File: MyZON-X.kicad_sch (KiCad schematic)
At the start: 29 parts, among them J1 Connector ZX81, SW1 SW_DIP_x03, U1 AY-3-8910, U2. 74HCT74, U3. 74HCT08, U4 74HCT11, U4. 74HCT11, U5. 74HCT02

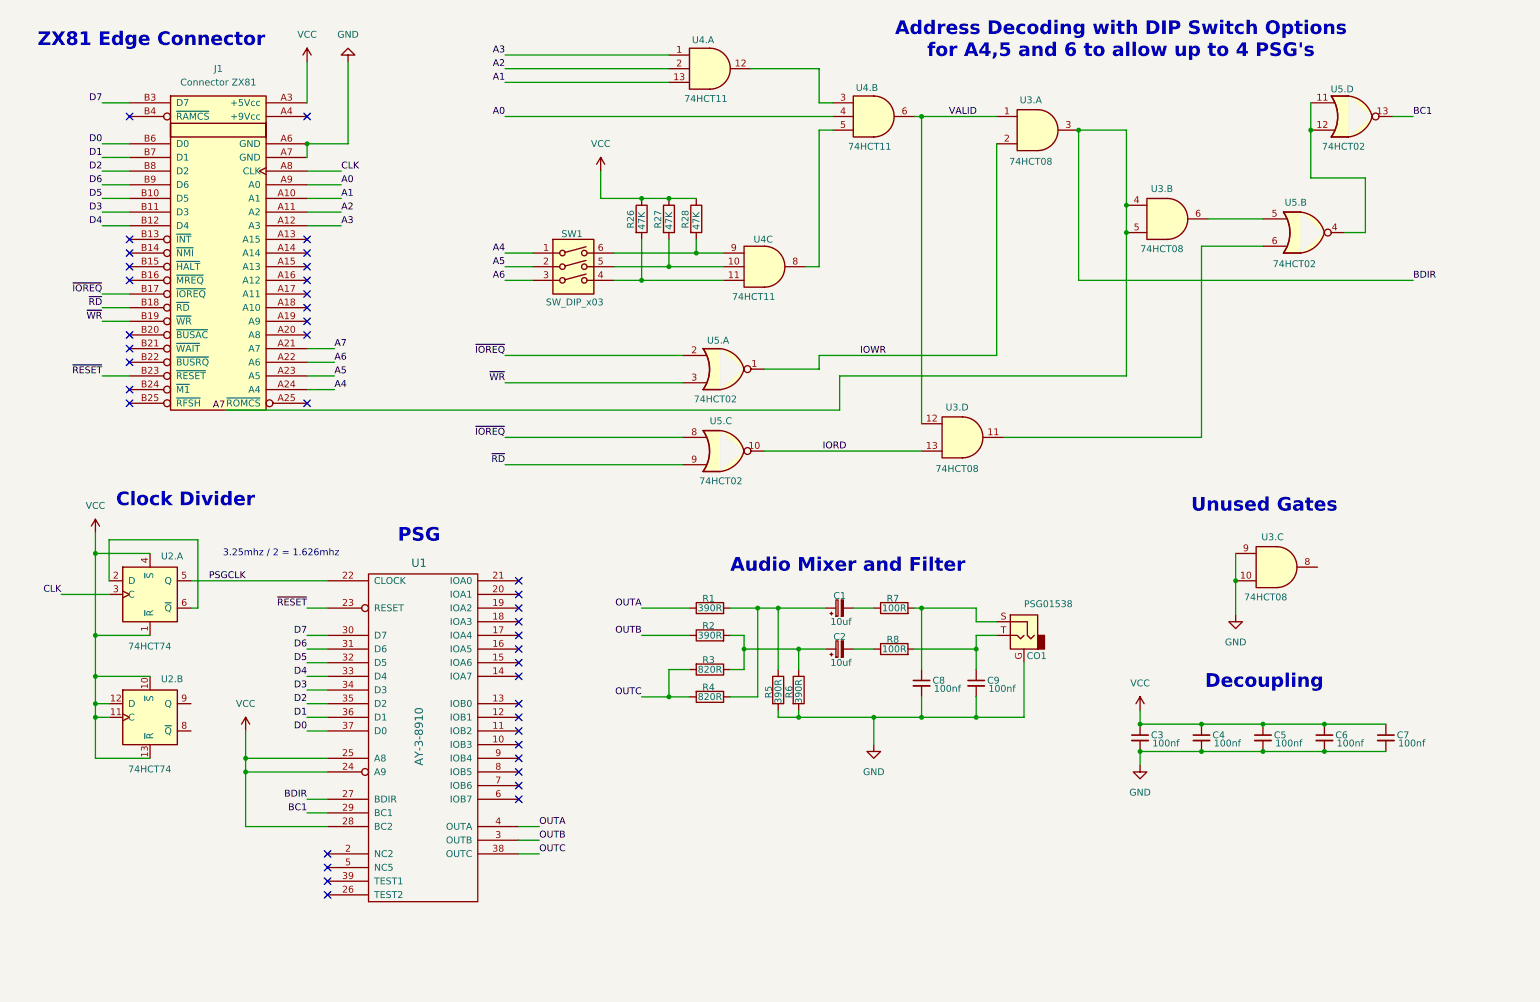
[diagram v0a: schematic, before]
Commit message: A7 was missaligned Added text to show detail of channel mixing on audio
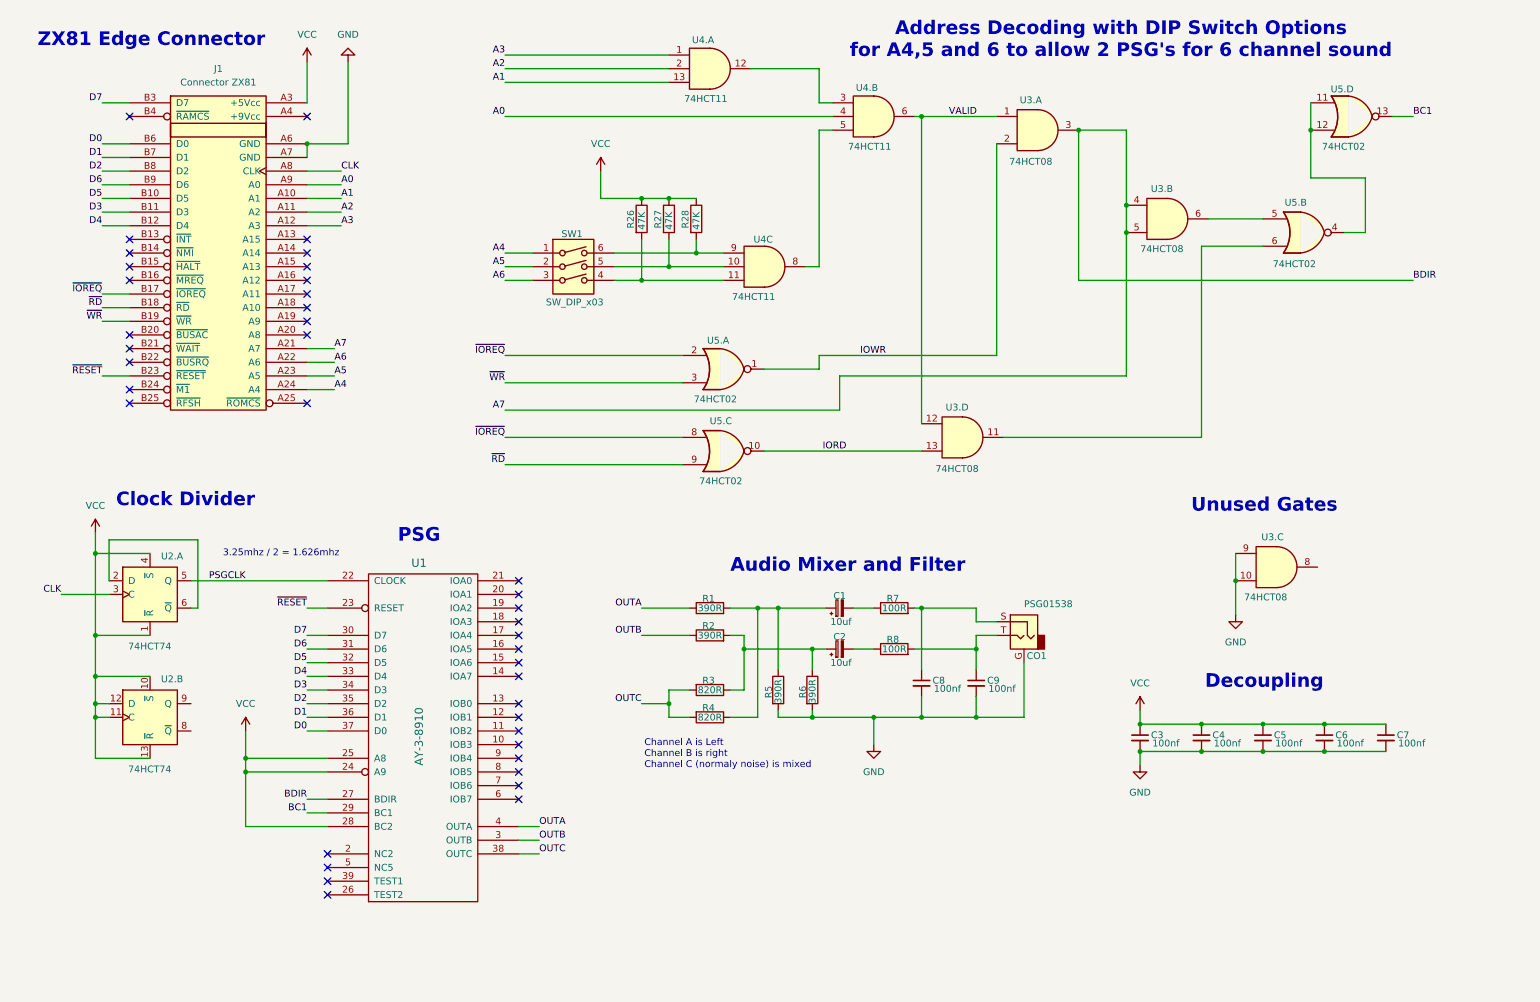
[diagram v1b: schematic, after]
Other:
- note added: "Address Decoding with DIP Switch Options for A4,5 and 6 to allow 2 PSG's for 6 channel sound"
- note added: "Channel A is Left Channel B is right Channel C (normaly noise) is mixed"
- note removed: "Address Decoding with DIP Switch Options for A4,5 and 6 to allow up to 4 PSG's"
- moved on the sheet: R3, R4, R6
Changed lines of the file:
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@@
 		(rev "1.0")
 	)
-	(text "Address Decoding with DIP Switch Options \nfor A4,5 and 6 to allow up to 4 PSG's"
+	(text "Address Decoding with DIP Switch Options \nfor A4,5 and 6 to allow 2 PSG's for 6 channel sound"
 		(exclude_from_sim no)
 		(at 219.964 20.066 0)
@@
 		)
 	)
+	(text "Channel A is Left\nChannel B is right\nChannel C (normaly noise) is mixed"
+		(exclude_from_sim no)
+		(at 131.318 152.908 0)
+		(effects
+			(font
+				(size 1.27 1.27)
+			)
+			(justify left)
+		)
+	)
 	(text "Audio Mixer and Filter"
 		(exclude_from_sim no)
@@
 	)
 	(junction
-		(at 135.89 142.24)
-		(diameter 0)
-		(color 0 0 0 0)
-	)
-	(junction
-		(at 160.02 133.35)
-		(diameter 0)
-		(color 0 0 0 0)
-	)
-	(junction
 		(at 135.89 49.53)
 		(diameter 0)
@@
 	)
 	(junction
-		(at 220.98 55.88)
+		(at 162.56 146.05)
 		(diameter 0)
 		(color 0 0 0 0)
 	)
 	(junction
-		(at 193.04 133.35)
+		(at 220.98 55.88)
 		(diameter 0)
 		(color 0 0 0 0)
 	)
 	(junction
-		(at 246.38 152.4)
+		(at 193.04 133.35)
 		(diameter 0)
 		(color 0 0 0 0)
 	)
 	(junction
-		(at 160.02 146.05)
+		(at 246.38 152.4)
 		(diameter 0)
 		(color 0 0 0 0)
@@
 	)
 	(junction
+		(at 135.89 143.51)
+		(diameter 0)
+		(color 0 0 0 0)
+	)
+	(junction
+		(at 162.56 133.35)
+		(diameter 0)
+		(color 0 0 0 0)
+	)
+	(junction
 		(at 182.88 34.29)
 		(diameter 0)
@@
 	(wire
 		(pts
-			(xy 149.86 137.16) (xy 149.86 133.35)
+			(xy 149.86 140.97) (xy 149.86 133.35)
 		)
 		(stroke
@@
 	(wire
 		(pts
-			(xy 160.02 133.35) (xy 165.1 133.35)
-		)
-		(stroke
-			(width 0)
-			(type default)
-		)
-	)
-	(wire
-		(pts
-			(xy 147.32 137.16) (xy 149.86 137.16)
+			(xy 147.32 140.97) (xy 149.86 140.97)
 		)
 		(stroke
@@
 	(wire
 		(pts
-			(xy 135.89 137.16) (xy 135.89 142.24)
+			(xy 162.56 133.35) (xy 165.1 133.35)
 		)
 		(stroke
@@
 	(wire
 		(pts
-			(xy 160.02 137.16) (xy 160.02 133.35)
-		)
-		(stroke
-			(width 0)
-			(type default)
-		)
-	)
-	(wire
-		(pts
-			(xy 160.02 146.05) (xy 173.99 146.05)
+			(xy 162.56 137.16) (xy 162.56 133.35)
 		)
 		(stroke
@@
 	(wire
 		(pts
-			(xy 149.86 133.35) (xy 160.02 133.35)
+			(xy 149.86 133.35) (xy 162.56 133.35)
 		)
 		(stroke
@@
 	(wire
 		(pts
-			(xy 156.21 146.05) (xy 160.02 146.05)
+			(xy 156.21 146.05) (xy 162.56 146.05)
 		)
 		(stroke
@@
 	(wire
 		(pts
+			(xy 162.56 146.05) (xy 173.99 146.05)
+		)
+		(stroke
+			(width 0)
+			(type default)
+		)
+	)
+	(wire
+		(pts
 			(xy 193.04 146.05) (xy 201.93 146.05)
 		)
@@
 	(wire
 		(pts
-			(xy 130.81 142.24) (xy 135.89 142.24)
+			(xy 130.81 143.51) (xy 135.89 143.51)
 		)
 		(stroke
@@
 	(wire
 		(pts
-			(xy 167.64 88.9) (xy 53.34 88.9)
+			(xy 167.64 88.9) (xy 105.41 88.9)
 		)
 		(stroke
@@
 	(wire
 		(pts
-			(xy 147.32 142.24) (xy 152.4 142.24)
+			(xy 147.32 146.05) (xy 152.4 146.05)
 		)
 		(stroke
@@
 	(wire
 		(pts
+			(xy 135.89 140.97) (xy 135.89 143.51)
+		)
+		(stroke
+			(width 0)
+			(type default)
+		)
+	)
+	(wire
+		(pts
 			(xy 31.75 113.03) (xy 48.26 113.03)
 		)
@@
 	(wire
 		(pts
-			(xy 160.02 144.78) (xy 160.02 146.05)
+			(xy 162.56 144.78) (xy 162.56 146.05)
 		)
 		(stroke
@@
 	(wire
 		(pts
-			(xy 152.4 142.24) (xy 152.4 125.73)
+			(xy 152.4 146.05) (xy 152.4 125.73)
 		)
 		(stroke
@@
 	(wire
 		(pts
-			(xy 135.89 142.24) (xy 139.7 142.24)
+			(xy 135.89 146.05) (xy 139.7 146.05)
 		)
 		(stroke
@@
 	(wire
 		(pts
+			(xy 135.89 146.05) (xy 135.89 143.51)
+		)
+		(stroke
+			(width 0)
+			(type default)
+		)
+	)
+	(wire
+		(pts
 			(xy 111.76 168.91) (xy 107.95 168.91)
 		)
@@
 	(wire
 		(pts
-			(xy 139.7 137.16) (xy 135.89 137.16)
+			(xy 139.7 140.97) (xy 135.89 140.97)
 		)
 		(stroke
@@
 	)
 	(label "A7"
-		(at 53.34 88.9 180)
+		(at 105.41 88.9 180)
 		(effects
 			(font
@@
 	)
 	(label "OUTC"
-		(at 130.81 142.24 180)
+		(at 130.81 143.51 180)
 		(effects
 			(font
@@
 		(lib_name "R_4")
 		(lib_id "Device:R")
-		(at 143.51 137.16 270)
+		(at 143.51 140.97 270)
 		(unit 1)
 		(exclude_from_sim no)
@@
 		(dnp no)
 		(property "Reference" "R3"
-			(at 143.256 135.382 90)
+			(at 143.256 139.192 90)
 			(effects
 				(font
@@
 		)
 		(property "Value" "820R"
-			(at 143.51 137.16 90)
+			(at 143.51 140.97 90)
 			(effects
 				(font
@@
 		)
 		(property "Footprint" ""
-			(at 143.51 135.382 90)
+			(at 143.51 139.192 90)
 			(effects
 				(font
@@
 		)
 		(property "Datasheet" "~"
-			(at 143.51 137.16 0)
+			(at 143.51 140.97 0)
 			(effects
 				(font
@@
 		)
 		(property "Description" "Resistor"
-			(at 143.51 137.16 0)
+			(at 143.51 140.97 0)
 			(effects
 				(font
@@
 		(lib_name "R_8")
 		(lib_id "Device:R")
-		(at 160.02 140.97 0)
+		(at 162.56 140.97 0)
 		(unit 1)
 		(exclude_from_sim no)
@@
 		(dnp no)
 		(property "Reference" "R6"
-			(at 158.242 142.494 90)
+			(at 160.782 142.494 90)
 			(effects
 				(font
@@
 		)
 		(property "Value" "390R"
-			(at 160.02 143.51 90)
+			(at 162.56 143.51 90)
 			(effects
 				(font
@@
 		)
 		(property "Footprint" ""
-			(at 158.242 140.97 90)
+			(at 160.782 140.97 90)
 			(effects
 				(font
@@
 		)
 		(property "Datasheet" "~"
-			(at 160.02 140.97 0)
+			(at 162.56 140.97 0)
 			(effects
 				(font
@@
 		)
 		(property "Description" "Resistor"
-			(at 160.02 140.97 0)
+			(at 162.56 140.97 0)
 			(effects
 				(font
@@
 		(lib_name "R_3")
 		(lib_id "Device:R")
-		(at 143.51 142.24 270)
+		(at 143.51 146.05 270)
 		(unit 1)
 		(exclude_from_sim no)
@@
 		(dnp no)
 		(property "Reference" "R4"
-			(at 143.256 140.462 90)
+			(at 143.256 144.272 90)
 			(effects
 				(font
@@
 		)
 		(property "Value" "820R"
-			(at 143.51 142.24 90)
+			(at 143.51 146.05 90)
 			(effects
 				(font
@@
 		)
 		(property "Footprint" ""
-			(at 143.51 140.462 90)
+			(at 143.51 144.272 90)
 			(effects
 				(font
@@
 		)
 		(property "Datasheet" "~"
-			(at 143.51 142.24 0)
+			(at 143.51 146.05 0)
 			(effects
 				(font
@@
 		)
 		(property "Description" "Resistor"
-			(at 143.51 142.24 0)
+			(at 143.51 146.05 0)
 			(effects
 				(font

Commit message: Added Audio interconnect Added extra nots for Addressing
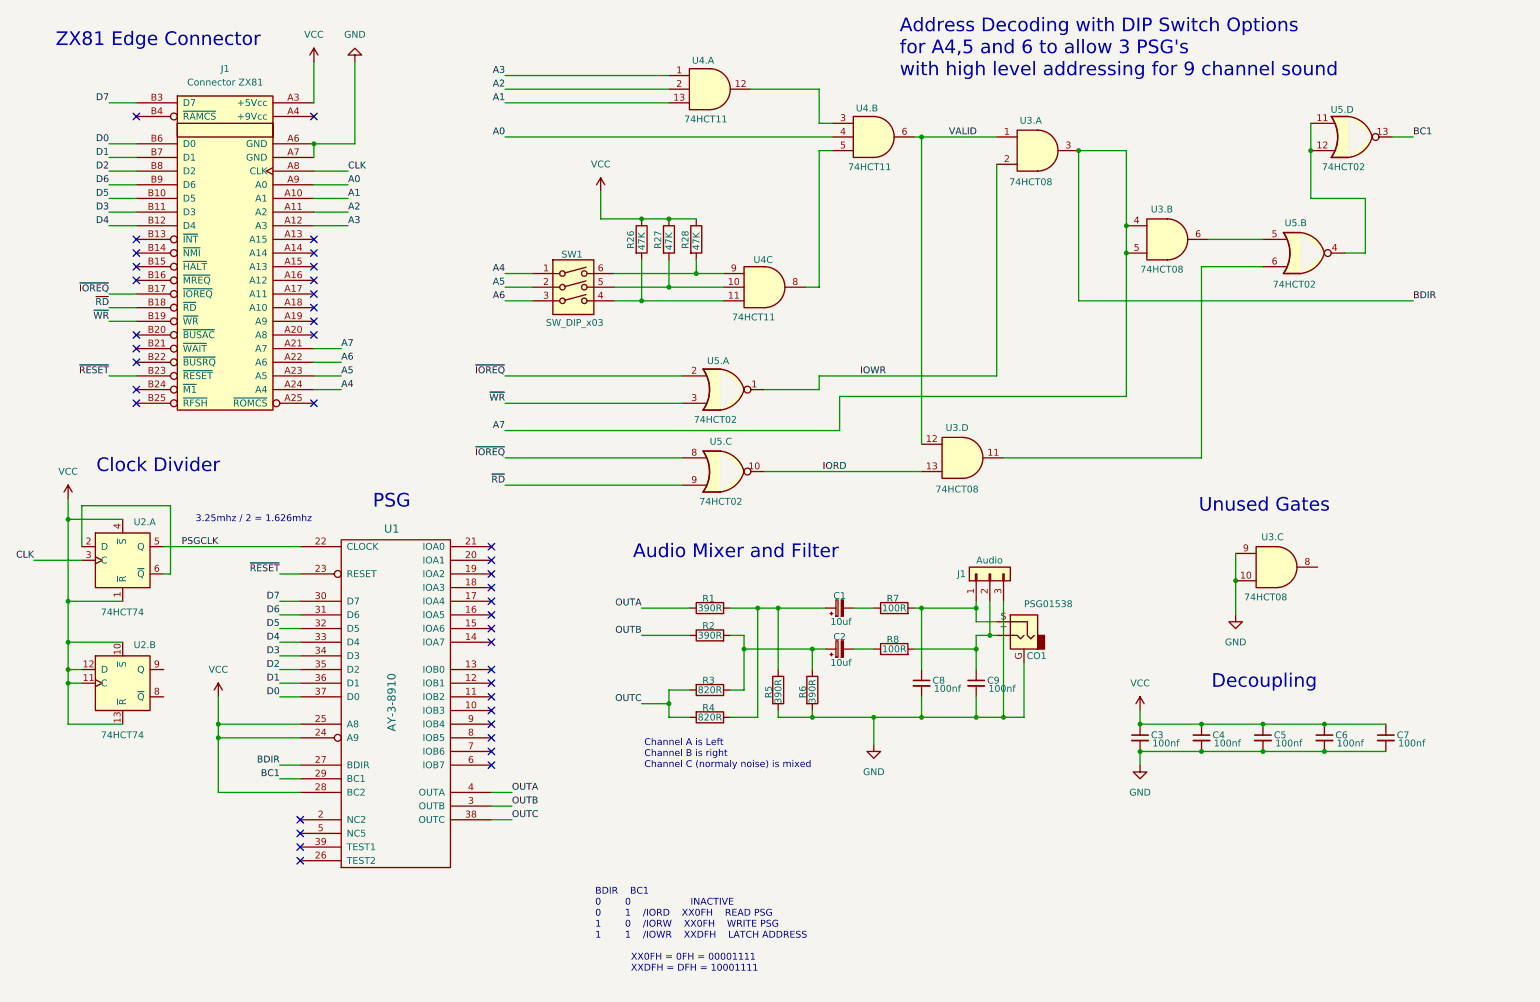
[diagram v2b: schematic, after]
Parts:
- added J1: Audio, symbol Connector_Generic:Conn_01x03
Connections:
- net GND: now also J1.3 (Pin_3)
- net at C9.1, CO1.T, R8.2: now also J1.2 (Pin_2)
- net at C8.1, CO1.S, R7.2: now also J1.1 (Pin_1)
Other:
- note added: "Address Decoding with DIP Switch Options for A4,5 and 6 to allow 3 PSG's with high level addressing for 9 channel sound"
- note added: "BDIR BC1 0 0 INACTIVE 0 1 /IORD XX0FH READ PSG 1 0 /IORW XX0FH WRITE PSG 1 1 /IOWR XXDFH LATCH ADDRESS XX0FH = 0FH = 00001111 XXDFH = DFH = 10001111"
- note removed: "Address Decoding with DIP Switch Options for A4,5 and 6 to allow 2 PSG's for 6 channel sound"
- moved on the sheet: J1, R26, R27, R28, SW1, U1, U2.A, U2.B, U3.A, U3.B, U3.D, U4.A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

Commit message: Added VCC and GND Added Power Suuply to IC's Commented 3 ERC warnings re bidirectional pins for 5v and GND for the ZX81 Connector
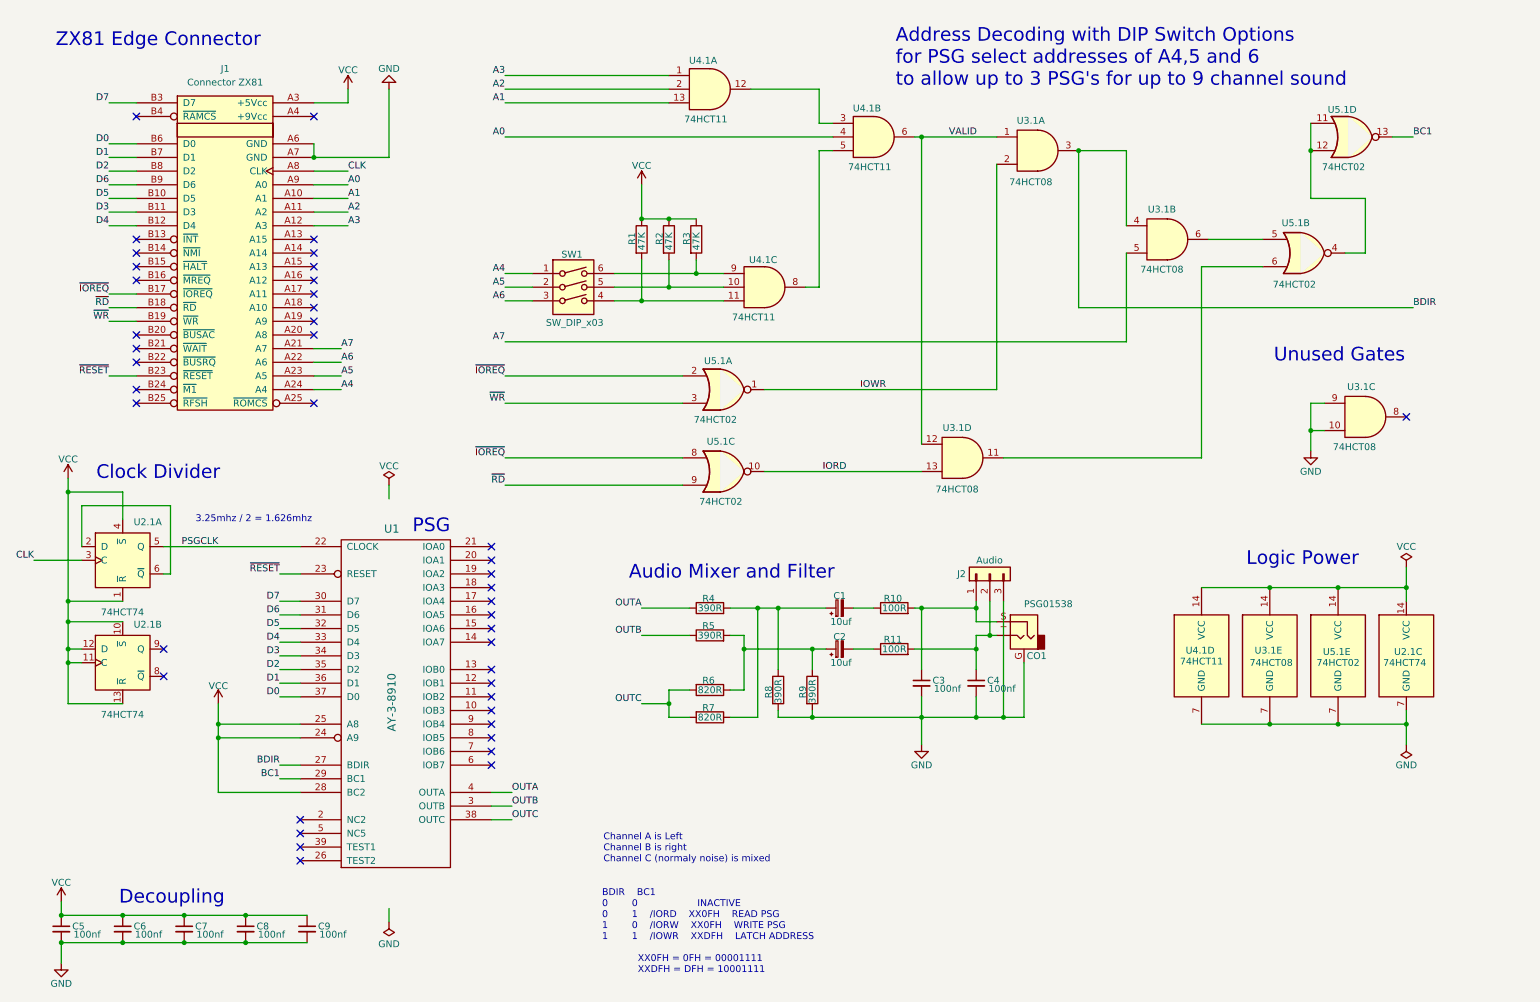
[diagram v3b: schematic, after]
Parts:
- removed R26, R27, R28: 47K, symbol Device:R
- added R1, R2, R3: 47K, symbol Device:R
- added unit 3 of U2.1
- added unit 5 of U3.1
- added unit 4 of U4.1
- added unit 5 of U5.1
- renumbered C8 to C3, C9 to C4, C3 to C5, C4 to C6, C5 to C7, C6 to C8, C7 to C9, J1 to J2, R7 to R10, R8 to R11, R1 to R4, R2 to R5, R3 to R6, R4 to R7, R5 to R8, R6 to R9, U2. to U2.1, U3. to U3.1, U4 to U4.1, U4. to U4.1, U5. to U5.1
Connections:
- net A7: no longer U1.27 (BDIR), U3.1.3, U3.1.4
- net VCC: now also R1.1, R2.1, R3.1
- net at SW1.4, U4.1.11: now also R1.2
- net at SW1.5, U4.1.10: now also R2.2
- net at SW1.6, U4.1.9: now also R3.2
- new net: U2.1.14 (VCC), U3.1.14 (VCC), U4.1.14 (VCC), U5.1.14 (VCC)
- new net: U2.1.7 (GND), U3.1.7 (GND), U4.1.7 (GND), U5.1.7 (GND)
- new net BDIR: U1.27 (BDIR), U3.1.3, U3.1.4
- no-connect marks 40 -> 43
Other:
- note added: "Address Decoding with DIP Switch Options for PSG select addresses of A4,5 and 6 to allow up to 3 PSG's for up to 9 channel sound"
- note added: "Logic Power"
- note removed: "Address Decoding with DIP Switch Options for A4,5 and 6 to allow 3 PSG's with high level addressing for 9 channel sound"
- moved on the sheet: C5, C6, C7, C8, C9, U2.1B, U3.1C
